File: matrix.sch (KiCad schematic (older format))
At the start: 46 parts

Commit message: v0.2
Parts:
- added D18, D24: 1N4148, symbol DIODE
- added S171, S18, S181, S191, S201, S211, S24, S51: MX1A, symbol MX1A
- renumbered D18 to D19, D19 to D23, S18 to S19, S19 to S23
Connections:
- net col1: now also D21.1 (A), D5.2 (K); no longer D23.1 (A), D5.1 (A)
- net col2: now also D22.1 (A); no longer D20.1 (A)
- net col3: now also D23.1 (A); no longer D21.1 (A)
- net col4: now also D17.2 (K), D19.2 (K), D20.2 (K), D18.2 (K), D24.1 (A); no longer D17.1 (A), D19.1 (A), D22.1 (A)
- net row2: now also S171.1
- net row3: now also S18.1, S181.1
- net row4: now also S191.1
- net row5: now also S20.1, S201.1, S51.1
- net row6: now also S211.1, S24.1; no longer S20.1
- net at S17.2: now also D17.1 (A), S171.2; no longer D17.2 (K)
- net at S19.2: now also D19.1 (A), S191.2; no longer D19.2 (K)
- net at S5.2: now also D5.1 (A), S51.2; no longer D5.2 (K)
- net at S20.2: now also D20.1 (A), S201.2; no longer D20.2 (K)
- net at D21.2 (K), S21.2: now also S211.2
- new net: D18.1 (A), S18.2, S181.2
- new net: D24.2 (K), S24.2
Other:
- moved on the sheet: D17, D19, D20, D21, D22, D23, D5, S20, S21, S22, S23

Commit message: v0.12
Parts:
- R4: value 300 -> kΩ; footprint (none) -> through-hole
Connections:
- net col4: now also D17.1 (A), D18.1 (A), D19.1 (A), D20.1 (A); no longer D17.2 (K), D18.2 (K), D19.2 (K), D20.2 (K)
- net at S17.2, S171.2: now also D17.2 (K); no longer D17.1 (A)
- net at S19.2, S191.2: now also D19.2 (K); no longer D19.1 (A)
- net at S20.2, S201.2: now also D20.2 (K); no longer D20.1 (A)
- net at S18.2, S181.2: now also D18.2 (K); no longer D18.1 (A)
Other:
- note added: "Numlock LED"
- note added: "Resistor Value dependent upon LED value"
- moved on the sheet: D17, DC1, R4
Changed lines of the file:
@@
-EESchema Schematic File Version 2  date 10/20/2013 1:26:13 PM
+EESchema Schematic File Version 2  date 11/25/2013 6:24:37 PM
 LIBS:power
 LIBS:mx1a-simple
@@
 LIBS:usb_ports
 LIBS:mechanical
+LIBS:mcp23018
+LIBS:component
 LIBS:keyboard-cache
 EELAYER 27 0
@@
 Sheet 2 2
 Title "4x6 keypad"
-Date "20 oct 2013"
-Rev "0.9"
+Date "25 nov 2013"
+Rev "0.12"
 Comp "regack"
 Comment1 ""
@@
 L LED DC1
 U 1 1 5042BB59
-P 12550 4000
-F 0 "DC1" H 12550 4100 50  0000 C CNN
-F 1 "LED" H 12550 3900 50  0000 C CNN
-F 2 "" H 12550 4000 60  0001 C CNN
-F 3 "" H 12550 4000 60  0001 C CNN
-	1    12550 4000
+P 7100 3900
+F 0 "DC1" H 7100 4000 50  0000 C CNN
+F 1 "LED" H 7100 3800 50  0000 C CNN
+F 2 "" H 7100 3900 60  0001 C CNN
+F 3 "" H 7100 3900 60  0001 C CNN
+	1    7100 3900
 	0    1    1    0
 $EndComp
@@
 col4
 $Comp
-L VCC #PWR030
+L VCC #PWR034
 U 1 1 5043970C
-P 12550 3550
-F 0 "#PWR030" H 12550 3650 30  0001 C CNN
-F 1 "VCC" H 12550 3650 30  0000 C CNN
-F 2 "" H 12550 3550 60  0001 C CNN
-F 3 "" H 12550 3550 60  0001 C CNN
-	1    12550 3550
+P 7100 3450
+F 0 "#PWR034" H 7100 3550 30  0001 C CNN
+F 1 "VCC" H 7100 3550 30  0000 C CNN
+F 2 "" H 7100 3450 60  0001 C CNN
+F 3 "" H 7100 3450 60  0001 C CNN
+	1    7100 3450
 	1    0    0    -1
 $EndComp
@@
 L R R4
 U 1 1 5043A0D0
-P 12550 4700
-F 0 "R4" V 12630 4700 50  0000 C CNN
-F 1 "300" V 12550 4700 50  0000 C CNN
-F 2 "" H 12550 4700 60  0001 C CNN
-F 3 "" H 12550 4700 60  0001 C CNN
-	1    12550 4700
+P 7100 4600
+F 0 "R4" V 7180 4600 50  0000 C CNN
+F 1 "kΩ" V 7100 4600 50  0000 C CNN
+F 2 "through-hole" H 7100 4600 60  0001 C CNN
+F 3 "Value depends on DC1 LED" H 7100 4600 60  0001 C CNN
+	1    7100 4600
 	1    0    0    -1
 $EndComp
@@
 L DIODE D17
 U 1 1 506B4394
-P 5450 5000
-F 0 "D17" H 5300 4950 40  0000 C CNN
-F 1 "1N4148" H 5350 5000 40  0000 C CNN
-F 2 "" H 5450 5000 60  0001 C CNN
-F 3 "" H 5450 5000 60  0001 C CNN
-F 4 "DC Components" H 3800 4400 60  0001 C CNN "Vendor"
-F 5 "CD4148WS(0805C)" H 3800 4400 60  0001 C CNN "Product"
-F 6 "TME" H 3800 4400 60  0001 C CNN "Supplier"
-F 7 "1N4148-0805" H 3800 4400 60  0001 C CNN "Supplier Symbol"
-	1    5450 5000
+P 5450 4900
+F 0 "D17" H 5300 4850 40  0000 C CNN
+F 1 "1N4148" H 5350 4900 40  0000 C CNN
+F 2 "" H 5450 4900 60  0001 C CNN
+F 3 "" H 5450 4900 60  0001 C CNN
+F 4 "DC Components" H 3800 4300 60  0001 C CNN "Vendor"
+F 5 "CD4148WS(0805C)" H 3800 4300 60  0001 C CNN "Product"
+F 6 "TME" H 3800 4300 60  0001 C CNN "Supplier"
+F 7 "1N4148-0805" H 3800 4300 60  0001 C CNN "Supplier Symbol"
+	1    5450 4900
 	1    0    0    -1
 $EndComp
@@
 Connection ~ 3100 5150
 Wire Wire Line
-	12550 3550 12550 3800
-Wire Wire Line
-	12550 4200 12550 4450
-Wire Wire Line
-	12550 4950 12550 5350
+	7100 3450 7100 3700
+Wire Wire Line
+	7100 4100 7100 4350
+Wire Wire Line
+	7100 4850 7100 5250
 Wire Wire Line
 	3850 3350 3850 3450
@@
 Wire Wire Line
 	5650 3350 5650 3200
-Wire Wire Line
-	5650 4400 5650 4900
 Connection ~ 5250 2950
 Connection ~ 5250 4150
@@
 Connection ~ 5700 3450
 Wire Wire Line
-	5700 1400 5700 9700
-Wire Wire Line
 	5000 1400 5000 9700
 Wire Wire Line
@@
 	3600 1400 3600 10150
 Wire Wire Line
-	5650 6900 5650 7400
+	5650 6900 5650 7500
 Connection ~ 5250 6650
 Text Notes 5300 7400 0    60   ~ 0
@@
 Wire Wire Line
 	1800 2950 5250 2950
-Text HLabel 12550 5350 2    60   3State ~ 0
+Text HLabel 7100 5250 2    60   3State ~ 0
 numlock
 $Comp
@@
 	3100 8400 3150 8400
 Connection ~ 3550 8650
-Connection ~ 5700 7500
 Connection ~ 5200 6650
 Wire Wire Line
@@
 Wire Wire Line
 	5200 6950 5250 6950
-Wire Wire Line
-	5650 7400 5250 7400
-Wire Wire Line
-	5250 7400 5250 7500
-Wire Wire Line
-	5650 7500 5700 7500
 Connection ~ 5650 7200
 Wire Wire Line
@@
 	5200 4450 5200 4150
 Connection ~ 5200 4150
-Wire Wire Line
-	5650 4900 5250 4900
-Wire Wire Line
-	5250 4900 5250 5000
 Connection ~ 5650 4700
-Wire Wire Line
-	5650 5000 5700 5000
-Connection ~ 5700 5000
 Text Notes 5350 8850 0    60   ~ 0
 FN
 Wire Wire Line
-	5650 8350 5650 8850
+	5650 8350 5650 8950
 Connection ~ 5250 8100
 $Comp
@@
 $EndComp
 Wire Wire Line
-	5650 5900 5650 5400
+	5650 5400 5650 6000
 $Comp
 L MX1A S24
@@
 	1    0    0    -1
 $EndComp
-Text Notes 5350 4900 0    60   ~ 0
+Text Notes 5350 4250 0    60   ~ 0
 PLUS
 Text Notes 5350 5900 0    60   ~ 0
@@
 	1    0    0    -1
 $EndComp
-Wire Wire Line
-	5250 5900 5650 5900
-Wire Wire Line
-	5250 5900 5250 6000
 Connection ~ 5650 5700
-Wire Wire Line
-	5650 6000 5700 6000
-Connection ~ 5700 6000
 Wire Wire Line
 	5250 5450 5200 5450
@@
 	5200 8400 5200 8100
 Connection ~ 5200 8100
-Wire Wire Line
-	5650 8850 5250 8850
-Wire Wire Line
-	5250 8850 5250 8950
 Connection ~ 5650 8650
-Wire Wire Line
-	5650 8950 5700 8950
-Connection ~ 5700 8950
 Wire Wire Line
 	4250 9450 4250 9600
 Connection ~ 5250 5150
 Connection ~ 3550 9750
+Wire Wire Line
+	5700 9700 5700 1400
+Wire Wire Line
+	5700 6100 5250 6100
+Wire Wire Line
+	5250 6100 5250 6000
+Connection ~ 5700 6100
+Wire Wire Line
+	5700 7600 5250 7600
+Wire Wire Line
+	5250 7600 5250 7500
+Connection ~ 5700 7600
+Wire Wire Line
+	5250 8950 5250 9050
+Wire Wire Line
+	5250 9050 5700 9050
+Connection ~ 5700 9050
+Wire Wire Line
+	5650 4400 5650 4900
+Wire Wire Line
+	5250 4900 5250 5000
+Wire Wire Line
+	5250 5000 5700 5000
+Connection ~ 5700 5000
+Text Notes 7300 4200 0    120  ~ 0
+Numlock LED
+Text Notes 7300 4600 0    120  ~ 0
+Resistor Value dependent upon LED value
 $EndSCHEMATC

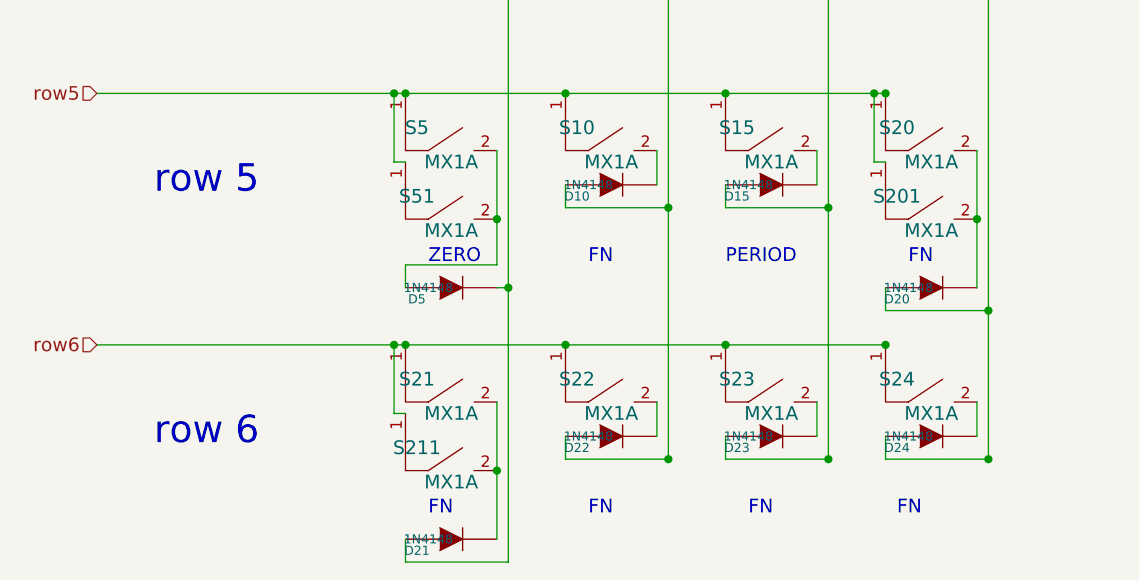
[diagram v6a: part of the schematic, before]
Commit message: 4x5 variant
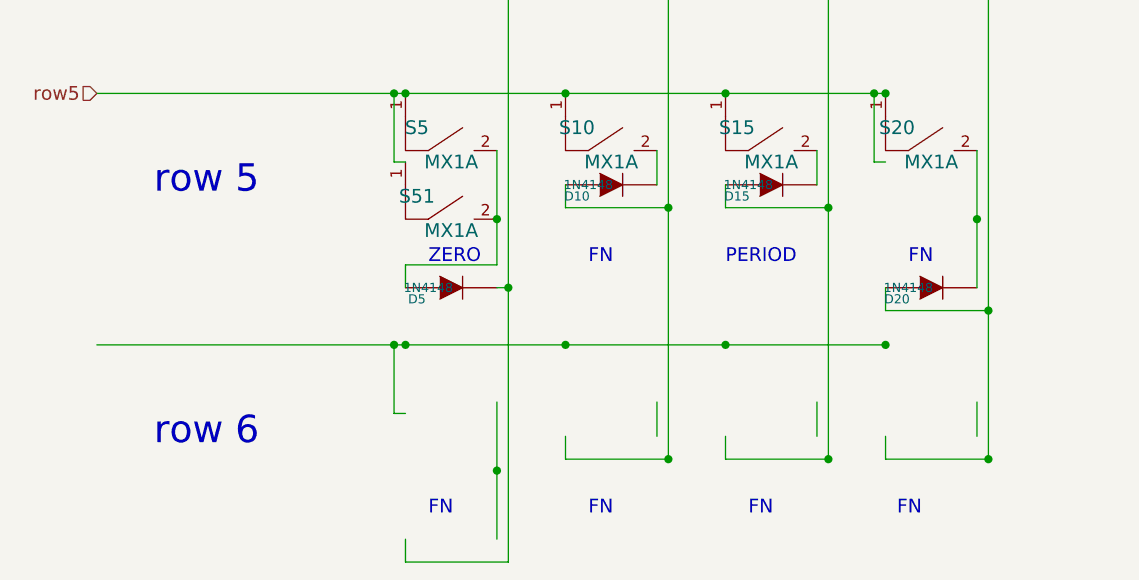
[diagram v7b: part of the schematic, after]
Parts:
- removed D21, D22, D23, D24: 1N4148, symbol DIODE
- removed S201, S21, S211, S22, S23, S24: MX1A, symbol MX1A
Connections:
- net labels removed: row6
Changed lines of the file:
@@
-EESchema Schematic File Version 2  date 12/16/2013 12:19:24 PM
+EESchema Schematic File Version 2  date 12/17/2013 3:58:37 PM
 LIBS:power
 LIBS:mx1a-simple
@@
 encoding utf-8
 Sheet 2 2
-Title "4x6 keypad"
-Date "25 nov 2013"
+Title "4x5 keypad"
+Date "17 dec 2013"
 Rev "0.12.1"
 Comp "regack"
@@
 	1    0    0    -1
 $EndComp
-$Comp
-L MX1A S21
-U 1 1 52376404
-P 3350 9600
-F 0 "S21" H 3200 9850 60  0000 C CNN
-F 1 "MX1A" H 3350 9700 60  0000 C CNN
-F 2 "" H 3350 9600 60  0001 C CNN
-F 3 "" H 3350 9600 60  0001 C CNN
-	1    3350 9600
-	1    0    0    -1
-$EndComp
-$Comp
-L MX1A S23
-U 1 1 5237640A
-P 4750 9600
-F 0 "S23" H 4600 9850 60  0000 C CNN
-F 1 "MX1A" H 4750 9700 60  0000 C CNN
-F 2 "" H 4750 9600 60  0001 C CNN
-F 3 "" H 4750 9600 60  0001 C CNN
-	1    4750 9600
-	1    0    0    -1
-$EndComp
 Text Notes 2050 9650 0    120  ~ 0
 row 6
-Text HLabel 1800 9200 0    60   Input ~ 0
-row6
-$Comp
-L DIODE D23
-U 1 1 52376416
-P 4750 9600
-F 0 "D23" H 4600 9550 40  0000 C CNN
-F 1 "1N4148" H 4650 9600 40  0000 C CNN
-F 2 "" H 4750 9600 60  0001 C CNN
-F 3 "" H 4750 9600 60  0001 C CNN
-F 4 "DC Components" H 4750 7000 60  0001 C CNN "Vendor"
-F 5 "CD4148WS(0805C)" H 4750 7000 60  0001 C CNN "Product"
-F 6 "TME" H 4750 7000 60  0001 C CNN "Supplier"
-F 7 "1N4148-0805" H 4750 7000 60  0001 C CNN "Supplier Symbol"
-	1    4750 9600
-	1    0    0    -1
-$EndComp
 $Comp
 L DIODE D20
@@
 	1    0    0    -1
 $EndComp
-$Comp
-L DIODE D21
-U 1 1 5237642A
-P 3350 10050
-F 0 "D21" H 3200 10000 40  0000 C CNN
-F 1 "1N4148" H 3250 10050 40  0000 C CNN
-F 2 "" H 3350 10050 60  0001 C CNN
-F 3 "" H 3350 10050 60  0001 C CNN
-F 4 "DC Components" H 2250 7750 60  0001 C CNN "Vendor"
-F 5 "CD4148WS(0805C)" H 2250 7750 60  0001 C CNN "Product"
-F 6 "TME" H 2250 7750 60  0001 C CNN "Supplier"
-F 7 "1N4148-0805" H 2250 7750 60  0001 C CNN "Supplier Symbol"
-	1    3350 10050
-	1    0    0    -1
-$EndComp
 Text Notes 3250 9950 0    60   ~ 0
 FN
@@
 Wire Wire Line
 	3550 9450 3550 10050
-$Comp
-L MX1A S22
-U 1 1 52376443
-P 4050 9600
-F 0 "S22" H 3900 9850 60  0000 C CNN
-F 1 "MX1A" H 4050 9700 60  0000 C CNN
-F 2 "" H 4050 9600 60  0001 C CNN
-F 3 "" H 4050 9600 60  0001 C CNN
-	1    4050 9600
-	1    0    0    -1
-$EndComp
-$Comp
-L DIODE D22
-U 1 1 5237644D
-P 4050 9600
-F 0 "D22" H 3900 9550 40  0000 C CNN
-F 1 "1N4148" H 3950 9600 40  0000 C CNN
-F 2 "" H 4050 9600 60  0001 C CNN
-F 3 "" H 4050 9600 60  0001 C CNN
-F 4 "DC Components" H 2400 8400 60  0001 C CNN "Vendor"
-F 5 "CD4148WS(0805C)" H 2400 8400 60  0001 C CNN "Product"
-F 6 "TME" H 2400 8400 60  0001 C CNN "Supplier"
-F 7 "1N4148-0805" H 2400 8400 60  0001 C CNN "Supplier Symbol"
-	1    4050 9600
-	1    0    0    -1
-$EndComp
 Wire Wire Line
 	5250 9600 5250 9700
@@
 Wire Wire Line
 	5650 5400 5650 6000
-$Comp
-L MX1A S24
-U 1 1 5238B9DC
-P 5450 9600
-F 0 "S24" H 5300 9850 60  0000 C CNN
-F 1 "MX1A" H 5450 9700 60  0000 C CNN
-F 2 "" H 5450 9600 60  0001 C CNN
-F 3 "" H 5450 9600 60  0001 C CNN
-	1    5450 9600
-	1    0    0    -1
-$EndComp
-$Comp
-L DIODE D24
-U 1 1 5238B9E6
-P 5450 9600
-F 0 "D24" H 5300 9550 40  0000 C CNN
-F 1 "1N4148" H 5350 9600 40  0000 C CNN
-F 2 "" H 5450 9600 60  0001 C CNN
-F 3 "" H 5450 9600 60  0001 C CNN
-F 4 "DC Components" H 5450 7000 60  0001 C CNN "Vendor"
-F 5 "CD4148WS(0805C)" H 5450 7000 60  0001 C CNN "Product"
-F 6 "TME" H 5450 7000 60  0001 C CNN "Supplier"
-F 7 "1N4148-0805" H 5450 7000 60  0001 C CNN "Supplier Symbol"
-	1    5450 9600
-	1    0    0    -1
-$EndComp
 Text Notes 5350 4250 0    60   ~ 0
 PLUS
 Text Notes 5350 5900 0    60   ~ 0
 FN
-$Comp
-L MX1A S211
-U 1 1 5238BB97
-P 3350 9900
-F 0 "S211" H 3200 10150 60  0000 C CNN
-F 1 "MX1A" H 3350 10000 60  0000 C CNN
-F 2 "" H 3350 9900 60  0001 C CNN
-F 3 "" H 3350 9900 60  0001 C CNN
-	1    3350 9900
-	1    0    0    -1
-$EndComp
 Wire Wire Line
 	3150 10050 3150 10150
@@
 	5200 5450 5200 5150
 Connection ~ 5200 5150
-$Comp
-L MX1A S201
-U 1 1 5238C086
-P 5450 8800
-F 0 "S201" H 5300 9050 60  0000 C CNN
-F 1 "MX1A" H 5450 8900 60  0000 C CNN
-F 2 "" H 5450 8800 60  0001 C CNN
-F 3 "" H 5450 8800 60  0001 C CNN
-	1    5450 8800
-	1    0    0    -1
-$EndComp
 Wire Wire Line
 	5250 8400 5200 8400
